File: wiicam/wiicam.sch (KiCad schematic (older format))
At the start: 10 parts, among them J1 Conn_01x04_Male, U1 LF33_TO220, U2 wiimote_ir_camera, X1 ACO-xxxMHz

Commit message: Update with available SMD components
Change to SMD components and change the regulator to what I have on hand
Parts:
- removed U1: LF33_TO220, Package_TO_SOT_SMD:SOT-223, symbol Regulator_Linear:LF33_TO220
- removed X1: ACO-xxxMHz, Oscillator:Oscillator_DIP-14_LargePads, symbol Oscillator:ACO-xxxMHz
- added C1: 10uF, Capacitor_SMD:C_0805_2012Metric_Pad1.18x1.45mm_HandSolder, symbol Device:C
- added U1: AMS1117-3.3, Package_TO_SOT_SMD:SOT-223-3_TabPin2, symbol Regulator_Linear:AMS1117-3.3
- added X1: S53305-25.000-X, Oscillator:Oscillator_SMD_TXC_7C-4Pin_5.0x3.2mm_HandSoldering, symbol Oscillator:ASE-xxxMHz
- C2: renamed from C1; footprint Capacitor_THT:C_Disc_D3.0mm_W1.6mm_P2.50mm -> Capacitor_SMD:C_0805_2012Metric_Pad1.18x1.45mm_HandSolder
- C3: renamed from C2; footprint Capacitor_THT:C_Disc_D3.0mm_W1.6mm_P2.50mm -> Capacitor_SMD:C_0805_2012Metric_Pad1.18x1.45mm_HandSolder
- C4: renamed from C3; footprint Capacitor_THT:C_Disc_D3.0mm_W1.6mm_P2.50mm -> Capacitor_SMD:C_0805_2012Metric_Pad1.18x1.45mm_HandSolder
- R1, R2, R3: footprint Resistor_THT:R_Axial_DIN0204_L3.6mm_D1.6mm_P2.54mm_Vertical -> Resistor_SMD:R_0805_2012Metric_Pad1.20x1.40mm_HandSolder
- U2: symbol wiimote_ir_camera:wiimote_ir_camera -> wiicam-rescue:wiimote_ir_camera-wiimote_ir_camera
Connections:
- wire segments 40 -> 46
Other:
- moved on the sheet: C4
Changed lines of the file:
@@
 EESchema Schematic File Version 4
-LIBS:wiicam-cache
 EELAYER 30 0
 EELAYER END
@@
 F 0 "R1" H 3970 2846 50  0000 L CNN
 F 1 "2k7" H 3970 2755 50  0000 L CNN
-F 2 "Resistor_THT:R_Axial_DIN0204_L3.6mm_D1.6mm_P2.54mm_Vertical" V 3830 2800 50  0001 C CNN
+F 2 "Resistor_SMD:R_0805_2012Metric_Pad1.20x1.40mm_HandSolder" V 3830 2800 50  0001 C CNN
 F 3 "~" H 3900 2800 50  0001 C CNN
 	1    3900 2800
@@
 F 0 "R2" H 4220 2846 50  0000 L CNN
 F 1 "2k7" H 4220 2755 50  0000 L CNN
-F 2 "Resistor_THT:R_Axial_DIN0204_L3.6mm_D1.6mm_P2.54mm_Vertical" V 4080 2800 50  0001 C CNN
+F 2 "Resistor_SMD:R_0805_2012Metric_Pad1.20x1.40mm_HandSolder" V 4080 2800 50  0001 C CNN
 F 3 "~" H 4150 2800 50  0001 C CNN
 	1    4150 2800
@@
 	4150 2950 3900 2950
 $Comp
-L wiimote_ir_camera:wiimote_ir_camera U2
+L wiicam-rescue:wiimote_ir_camera-wiimote_ir_camera U2
 U 1 1 5DBBEB03
 P 6350 2550
@@
 Wire Wire Line
 	6100 2450 5350 2450
-Text GLabel 6050 2900 2    50   Output ~ 0
+Text GLabel 6750 2900 2    50   Output ~ 0
 CLK
 Text GLabel 5350 2250 0    50   Output ~ 0
@@
 F 0 "R3" H 4470 2846 50  0000 L CNN
 F 1 "33k" H 4470 2755 50  0000 L CNN
-F 2 "Resistor_THT:R_Axial_DIN0204_L3.6mm_D1.6mm_P2.54mm_Vertical" V 4330 2800 50  0001 C CNN
+F 2 "Resistor_SMD:R_0805_2012Metric_Pad1.20x1.40mm_HandSolder" V 4330 2800 50  0001 C CNN
 F 3 "~" H 4400 2800 50  0001 C CNN
 	1    4400 2800
@@
 	7550 2450 6600 2450
 $Comp
+L Device:C C4
+U 1 1 5DBC4357
+P 6600 3250
+F 0 "C4" H 6715 3296 50  0000 L CNN
+F 1 "10nF" H 6715 3205 50  0000 L CNN
+F 2 "Capacitor_SMD:C_0805_2012Metric_Pad1.18x1.45mm_HandSolder" H 6638 3100 50  0001 C CNN
+F 3 "~" H 6600 3250 50  0001 C CNN
+	1    6600 3250
+	1    0    0    -1
+$EndComp
+$Comp
 L Device:C C3
-U 1 1 5DBC4357
-P 5850 3250
-F 0 "C3" H 5965 3296 50  0000 L CNN
-F 1 "10nF" H 5965 3205 50  0000 L CNN
-F 2 "Capacitor_THT:C_Disc_D3.0mm_W1.6mm_P2.50mm" H 5888 3100 50  0001 C CNN
-F 3 "~" H 5850 3250 50  0001 C CNN
-	1    5850 3250
-	1    0    0    -1
-$EndComp
-$Comp
-L Device:C C2
 U 1 1 5DBC553F
 P 4850 3100
-F 0 "C2" H 4965 3146 50  0000 L CNN
+F 0 "C3" H 4965 3146 50  0000 L CNN
 F 1 "10nF" H 4965 3055 50  0000 L CNN
-F 2 "Capacitor_THT:C_Disc_D3.0mm_W1.6mm_P2.50mm" H 4888 2950 50  0001 C CNN
+F 2 "Capacitor_SMD:C_0805_2012Metric_Pad1.18x1.45mm_HandSolder" H 4888 2950 50  0001 C CNN
 F 3 "~" H 4850 3100 50  0001 C CNN
 	1    4850 3100
@@
 $EndComp
 Wire Wire Line
-	3150 3250 3550 3250
-Wire Wire Line
 	3450 2950 3550 2950
 Connection ~ 3900 2950
 $Comp
-L Device:C C1
+L Device:C C2
 U 1 1 5DBCA2C2
 P 3550 3100
-F 0 "C1" H 3665 3146 50  0000 L CNN
+F 0 "C2" H 3665 3146 50  0000 L CNN
 F 1 "10uF" H 3665 3055 50  0000 L CNN
-F 2 "Capacitor_THT:C_Disc_D3.0mm_W1.6mm_P2.50mm" H 3588 2950 50  0001 C CNN
+F 2 "Capacitor_SMD:C_0805_2012Metric_Pad1.18x1.45mm_HandSolder" H 3588 2950 50  0001 C CNN
 F 3 "~" H 3550 3100 50  0001 C CNN
 	1    3550 3100
@@
 Wire Wire Line
 	3550 2850 3550 2950
-$Comp
-L Oscillator:ACO-xxxMHz X1
-U 1 1 5DBD1A3A
-P 5350 3100
-F 0 "X1" H 5007 3146 50  0000 R CNN
-F 1 "ACO-xxxMHz" H 5007 3055 50  0000 R CNN
-F 2 "Oscillator:Oscillator_DIP-14_LargePads" H 5800 2750 50  0001 C CNN
-F 3 "http://www.conwin.com/datasheets/cx/cx030.pdf" H 5250 3100 50  0001 C CNN
-	1    5350 3100
-	1    0    0    -1
-$EndComp
 Wire Wire Line
 	4850 2950 4850 2800
-Wire Wire Line
-	4850 2800 5350 2800
 Connection ~ 4850 2950
-Wire Wire Line
-	4850 3250 4850 3400
-Wire Wire Line
-	4850 3400 5350 3400
 Connection ~ 4850 3250
 Wire Wire Line
-	5850 3400 5350 3400
-Connection ~ 5350 3400
-Wire Wire Line
-	5850 3100 5650 3100
-Wire Wire Line
-	5850 3100 5850 2900
-Wire Wire Line
-	5850 2900 6050 2900
-Connection ~ 5850 3100
-$Comp
-L Regulator_Linear:LF33_TO220 U1
-U 1 1 5DBC831E
-P 3150 2950
-F 0 "U1" H 3150 3192 50  0000 C CNN
-F 1 "LF33_TO220" H 3150 3101 50  0000 C CNN
-F 2 "Package_TO_SOT_SMD:SOT-223" H 3150 3175 50  0001 C CIN
-F 3 "http://www.st.com/content/ccc/resource/technical/document/datasheet/c4/0e/7e/2a/be/bc/4c/bd/CD00000546.pdf/files/CD00000546.pdf/jcr:content/translations/en.CD00000546.pdf" H 3150 2900 50  0001 C CNN
-	1    3150 2950
-	1    0    0    -1
-$EndComp
+	6600 3100 5950 3100
+Wire Wire Line
+	6600 3100 6600 2900
+Wire Wire Line
+	6600 2900 6750 2900
+Connection ~ 6600 3100
 Wire Wire Line
 	2850 2950 2700 2950
@@
 	2700 2950 2700 2450
 Wire Wire Line
-	3150 3250 2100 3250
-Wire Wire Line
 	2100 3250 2100 2550
-Connection ~ 3150 3250
 Wire Wire Line
 	3900 2350 3900 2650
@@
 	1    0    0    -1
 $EndComp
+$Comp
+L Regulator_Linear:AMS1117-3.3 U1
+U 1 1 626C201F
+P 3150 2950
+F 0 "U1" H 3150 3192 50  0000 C CNN
+F 1 "AMS1117-3.3" H 3150 3101 50  0000 C CNN
+F 2 "Package_TO_SOT_SMD:SOT-223-3_TabPin2" H 3150 3150 50  0001 C CNN
+F 3 "http://www.advanced-monolithic.com/pdf/ds1117.pdf" H 3250 2700 50  0001 C CNN
+	1    3150 2950
+	1    0    0    -1
+$EndComp
+Wire Wire Line
+	2100 3250 2700 3250
+Connection ~ 3150 3250
+Wire Wire Line
+	3150 3250 3550 3250
+$Comp
+L Device:C C1
+U 1 1 626C4A64
+P 2700 3100
+F 0 "C1" H 2500 3150 50  0000 L CNN
+F 1 "10uF" H 2400 3050 50  0000 L CNN
+F 2 "Capacitor_SMD:C_0805_2012Metric_Pad1.18x1.45mm_HandSolder" H 2738 2950 50  0001 C CNN
+F 3 "~" H 2700 3100 50  0001 C CNN
+	1    2700 3100
+	1    0    0    -1
+$EndComp
+Connection ~ 2700 2950
+Connection ~ 2700 3250
+Wire Wire Line
+	2700 3250 3150 3250
+$Comp
+L Oscillator:ASE-xxxMHz X1
+U 1 1 626C7E4D
+P 5650 3100
+F 0 "X1" H 5750 2850 50  0000 L CNN
+F 1 "S53305-25.000-X" H 5700 2700 50  0000 L CNN
+F 2 "Oscillator:Oscillator_SMD_TXC_7C-4Pin_5.0x3.2mm_HandSoldering" H 6350 2750 50  0001 C CNN
+F 3 "http://www.abracon.com/Oscillators/ASV.pdf" H 5550 3100 50  0001 C CNN
+	1    5650 3100
+	1    0    0    -1
+$EndComp
+Wire Wire Line
+	5350 3100 5250 3100
+Wire Wire Line
+	5250 3100 5250 2800
+Wire Wire Line
+	5250 2800 5650 2800
+Connection ~ 5250 2800
+Wire Wire Line
+	4850 2800 5250 2800
+Wire Wire Line
+	6600 3400 6600 3600
+Wire Wire Line
+	6600 3600 5650 3600
+Wire Wire Line
+	4850 3250 4850 3600
+Wire Wire Line
+	5650 3400 5650 3600
+Connection ~ 5650 3600
+Wire Wire Line
+	5650 3600 4850 3600
 $EndSCHEMATC

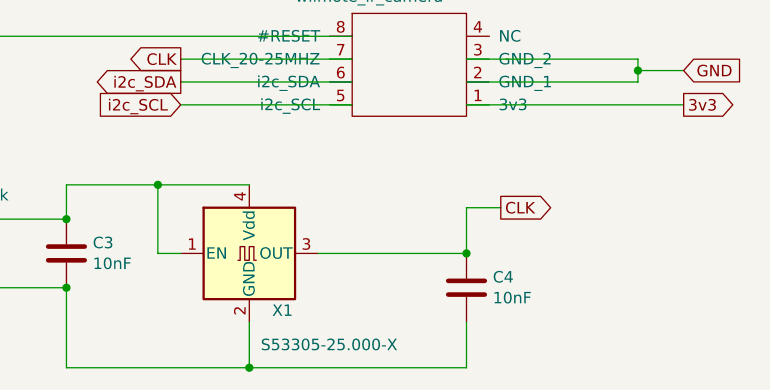
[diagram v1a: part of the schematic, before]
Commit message: Remove OSC output capacitor Output capacitor value is too high - S53305-25.000-X is rated at max 15pF output load
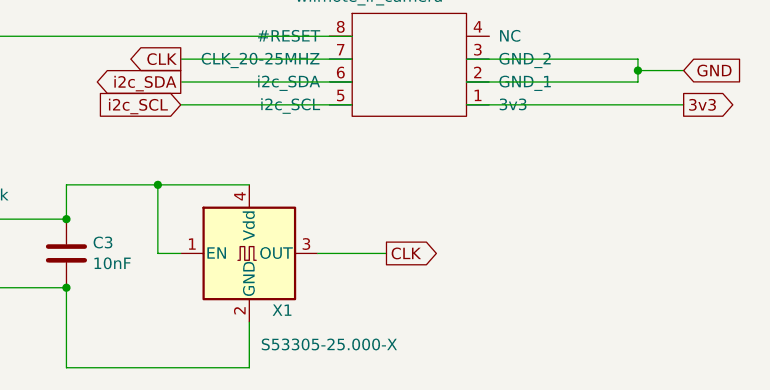
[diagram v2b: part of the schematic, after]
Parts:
- removed C4: 10nF, Capacitor_SMD:C_0805_2012Metric_Pad1.18x1.45mm_HandSolder, symbol Device:C
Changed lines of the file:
@@
 Wire Wire Line
 	6100 2450 5350 2450
-Text GLabel 6750 2900 2    50   Output ~ 0
+Text GLabel 6250 3100 2    50   Output ~ 0
 CLK
 Text GLabel 5350 2250 0    50   Output ~ 0
@@
 	7550 2450 6600 2450
 $Comp
-L Device:C C4
-U 1 1 5DBC4357
-P 6600 3250
-F 0 "C4" H 6715 3296 50  0000 L CNN
-F 1 "10nF" H 6715 3205 50  0000 L CNN
-F 2 "Capacitor_SMD:C_0805_2012Metric_Pad1.18x1.45mm_HandSolder" H 6638 3100 50  0001 C CNN
-F 3 "~" H 6600 3250 50  0001 C CNN
-	1    6600 3250
-	1    0    0    -1
-$EndComp
-$Comp
 L Device:C C3
 U 1 1 5DBC553F
@@
 Connection ~ 4850 3250
 Wire Wire Line
-	6600 3100 5950 3100
-Wire Wire Line
-	6600 3100 6600 2900
-Wire Wire Line
-	6600 2900 6750 2900
-Connection ~ 6600 3100
+	6250 3100 5950 3100
 Wire Wire Line
 	2850 2950 2700 2950
@@
 	4850 2800 5250 2800
 Wire Wire Line
-	6600 3400 6600 3600
-Wire Wire Line
-	6600 3600 5650 3600
-Wire Wire Line
 	4850 3250 4850 3600
 Wire Wire Line
 	5650 3400 5650 3600
-Connection ~ 5650 3600
 Wire Wire Line
 	5650 3600 4850 3600
